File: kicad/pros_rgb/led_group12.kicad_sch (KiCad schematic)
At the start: 8 parts

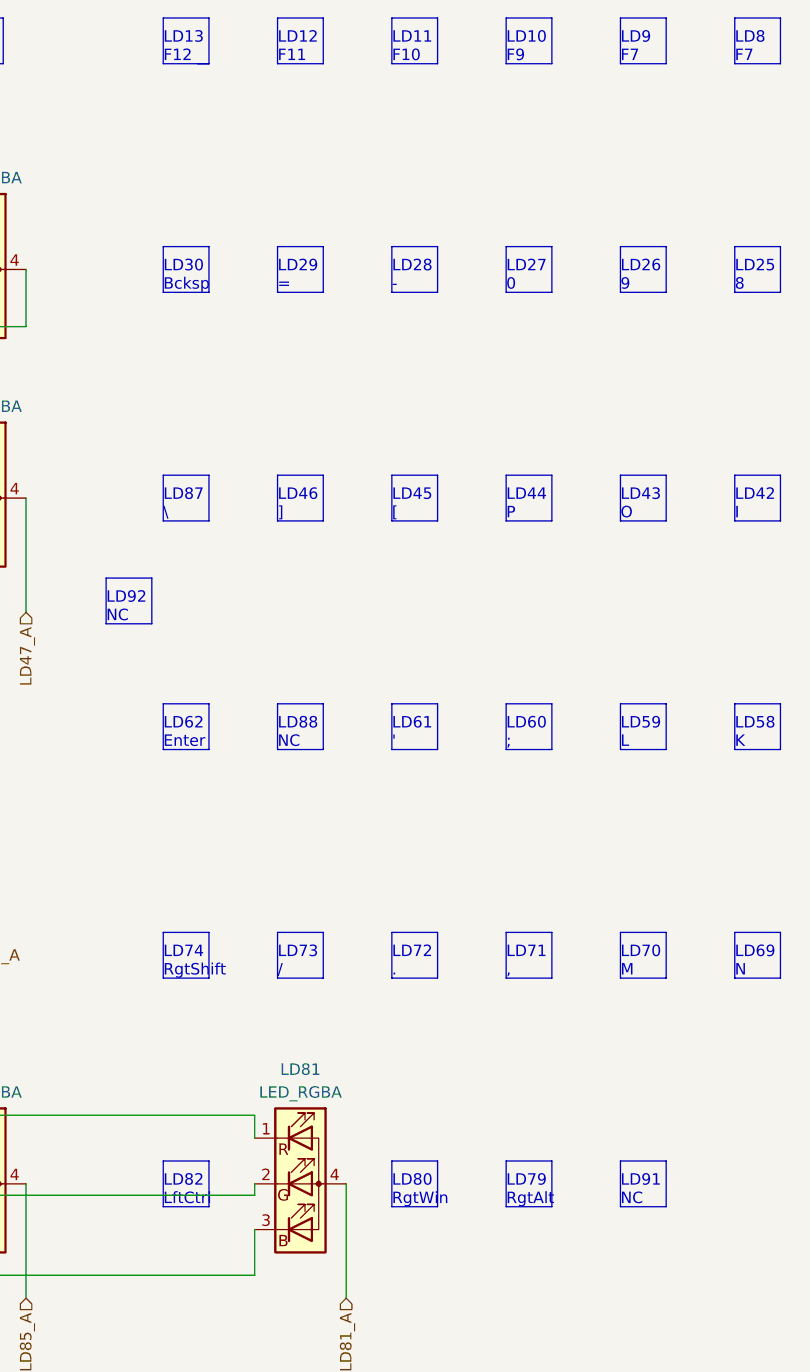
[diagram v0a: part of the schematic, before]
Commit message: kicad/pros_rgb: fix typos
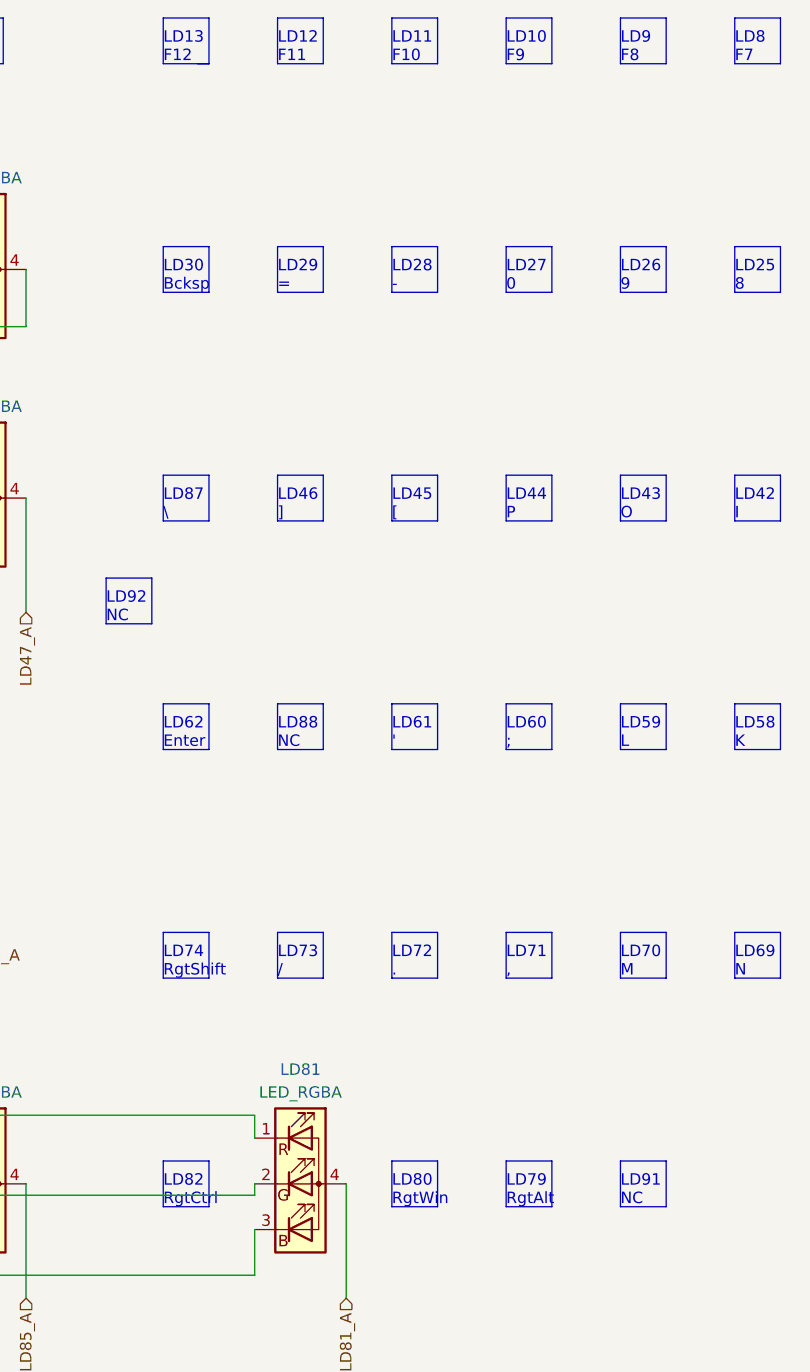
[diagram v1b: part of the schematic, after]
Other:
- note added: "LD82 RgtCtrl"
- note added: "LD9 F8"
- note removed: "LD82 LftCtrl"
- note removed: "LD9 F7"
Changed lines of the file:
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@@
     (effects (font (size 1.27 1.27)) (justify left bottom))
   )
-  (text "LD9\nF7" (at 157.48 29.21 0)
+  (text "LD9\nF8" (at 157.48 29.21 0)
     (effects (font (size 1.27 1.27)) (justify left bottom))
   )
@@
     (effects (font (size 1.27 1.27)) (justify left bottom))
   )
-  (text "LD82\nLftCtrl" (at 106.68 156.21 0)
+  (text "LD82\nRgtCtrl" (at 106.68 156.21 0)
     (effects (font (size 1.27 1.27)) (justify left bottom))
   )

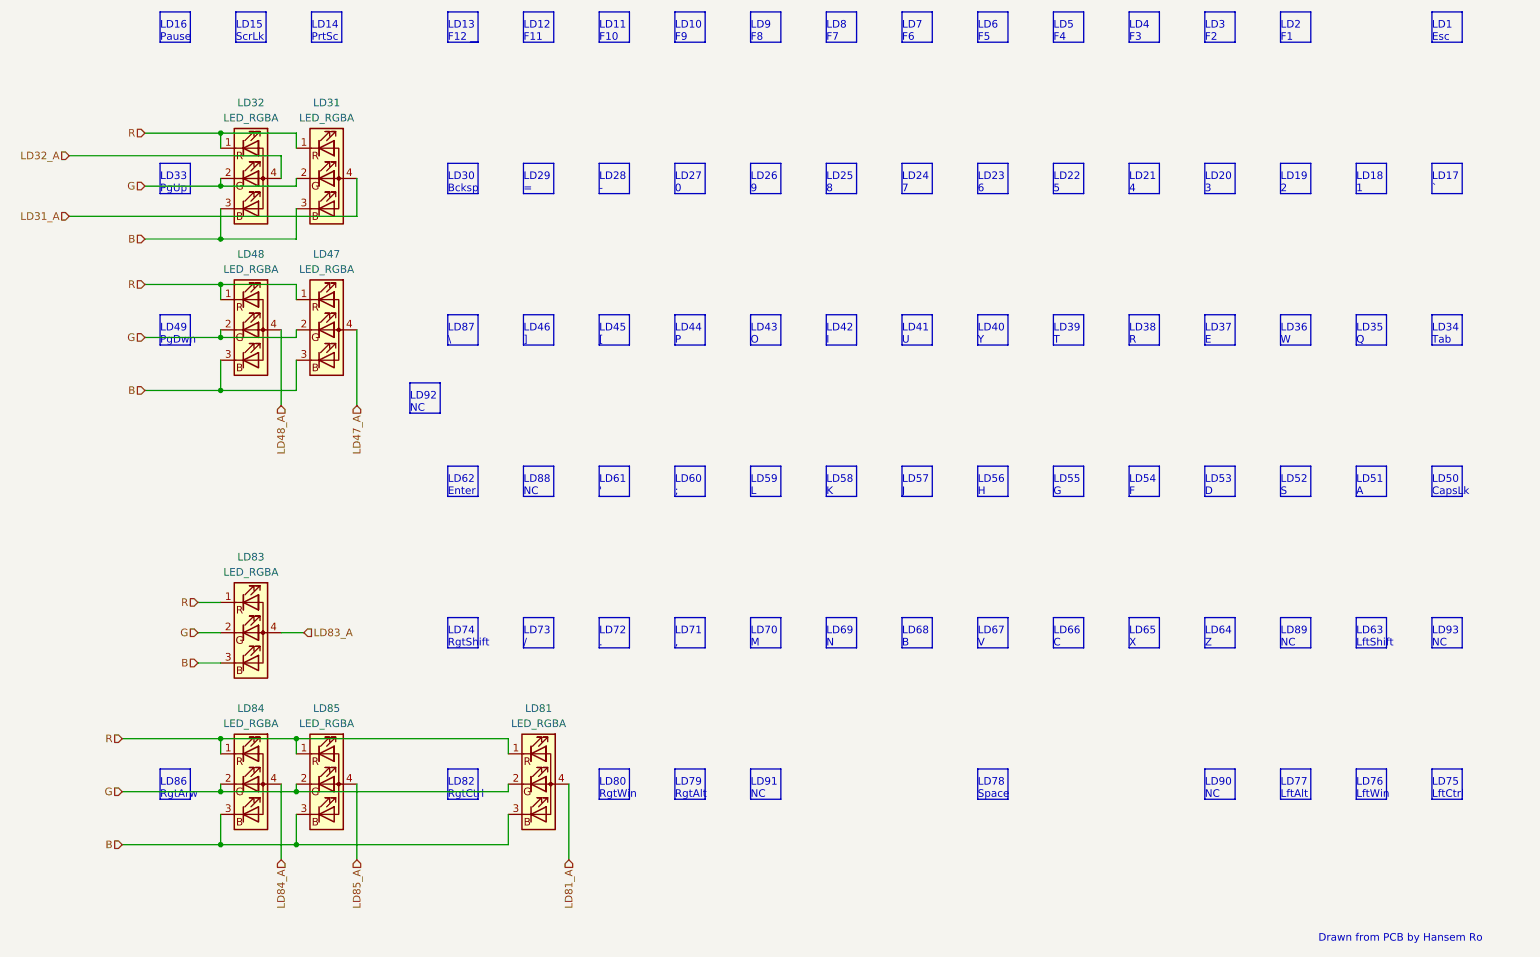
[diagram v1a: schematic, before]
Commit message: kicad/pros_rgb: order led groups by channel number
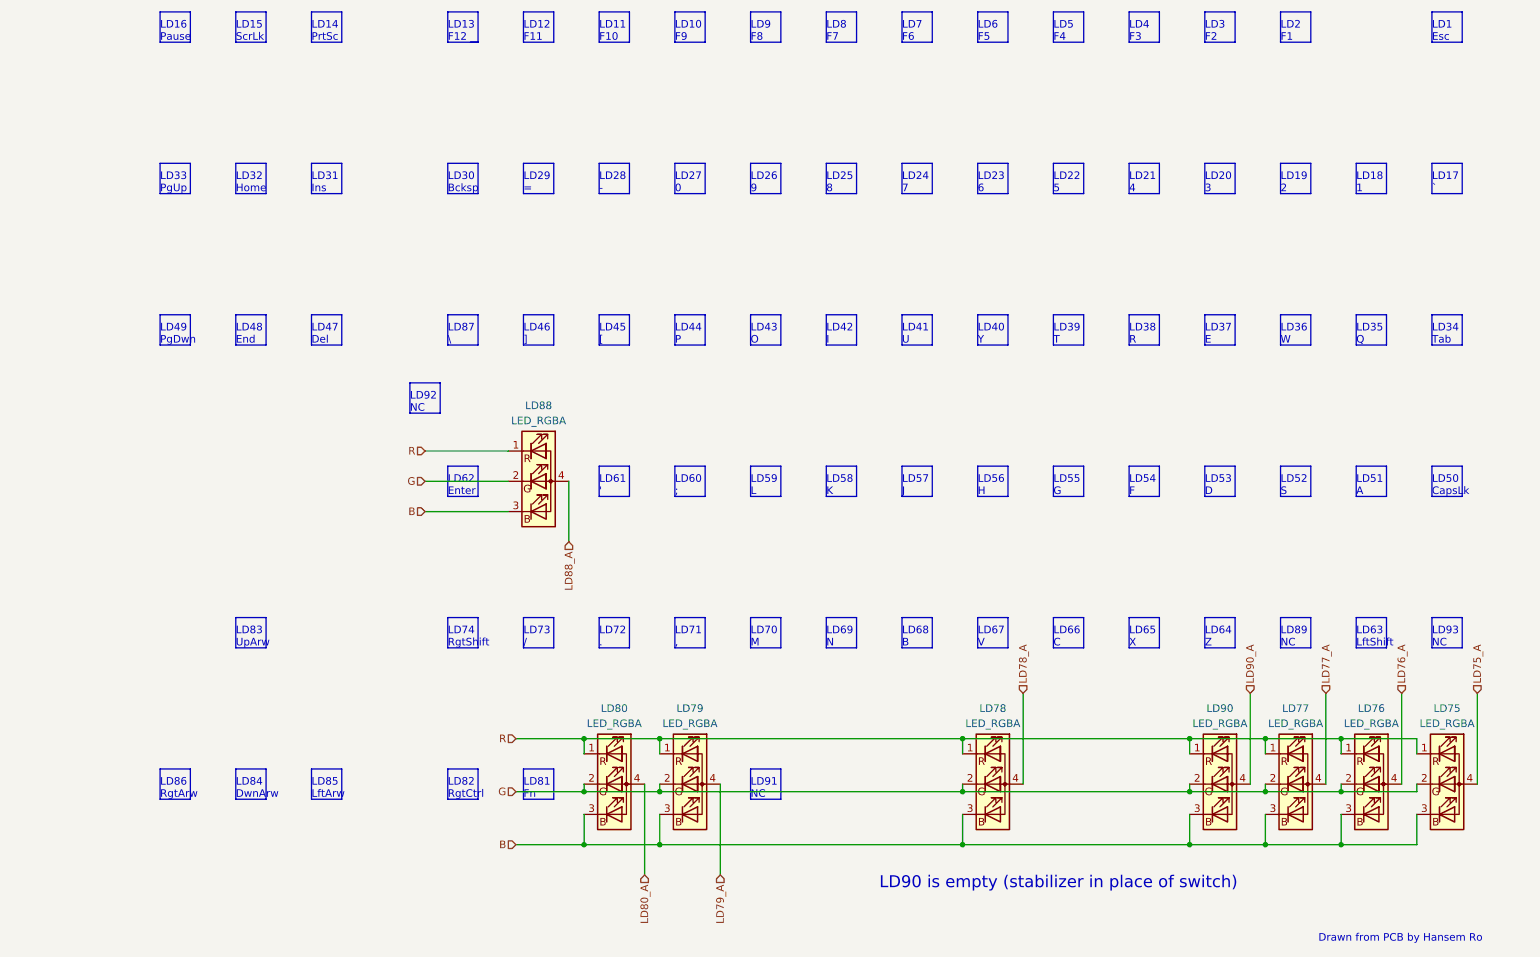
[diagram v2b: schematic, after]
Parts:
- removed LD31, LD32, LD47, LD48, LD81, LD83, LD84, LD85: LED_RGBA, symbol Device:LED_RGBA
- added LD75, LD76, LD77, LD78, LD79, LD80, LD88, LD90: LED_RGBA, symbol Device:LED_RGBA
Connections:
- net B: now also LD75.3 (BK), LD76.3 (BK), LD77.3 (BK), LD78.3 (BK), LD79.3 (BK), LD80.3 (BK), LD88.3 (BK), LD90.3 (BK)
- net G: now also LD75.2 (GK), LD76.2 (GK), LD77.2 (GK), LD78.2 (GK), LD79.2 (GK), LD80.2 (GK), LD88.2 (GK), LD90.2 (GK)
- net R: now also LD75.1 (RK), LD76.1 (RK), LD77.1 (RK), LD78.1 (RK), LD79.1 (RK), LD80.1 (RK), LD88.1 (RK), LD90.1 (RK)
- new net LD75_A: LD75.4 (A)
- new net LD76_A: LD76.4 (A)
- new net LD77_A: LD77.4 (A)
- new net LD78_A: LD78.4 (A)
- new net LD79_A: LD79.4 (A)
- new net LD80_A: LD80.4 (A)
- new net LD88_A: LD88.4 (A)
- new net LD90_A: LD90.4 (A)
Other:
- note added: "LD31 Ins"
- note added: "LD32 Home"
- note added: "LD47 Del"
- note added: "LD48 End"
- note added: "LD81 Fn"
- note added: "LD83 UpArw"
- note added: "LD84 DwnArw"
- note added: "LD85 LftArw"
- note added: "LD90 is empty (stabilizer in place of switch)"
- note removed: "LD75 LftCtrl"
- note removed: "LD76 LftWin"
- note removed: "LD77 LftAlt"
- note removed: "LD78 Space"
- note removed: "LD79 RgtAlt"
- note removed: "LD80 RgtWin"
- note removed: "LD88 NC"
- note removed: "LD90 NC"
